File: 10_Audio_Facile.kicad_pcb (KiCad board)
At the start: 2 copper layers, 30.5 x 20.3 mm, 20 parts, among them J1 Conn_01x01, J2 Conn_01x01, J3 Conn_01x01, J4 Conn_01x01, J5 Conn_01x01, J6 Conn_01x01, U1 PAM8302AAS

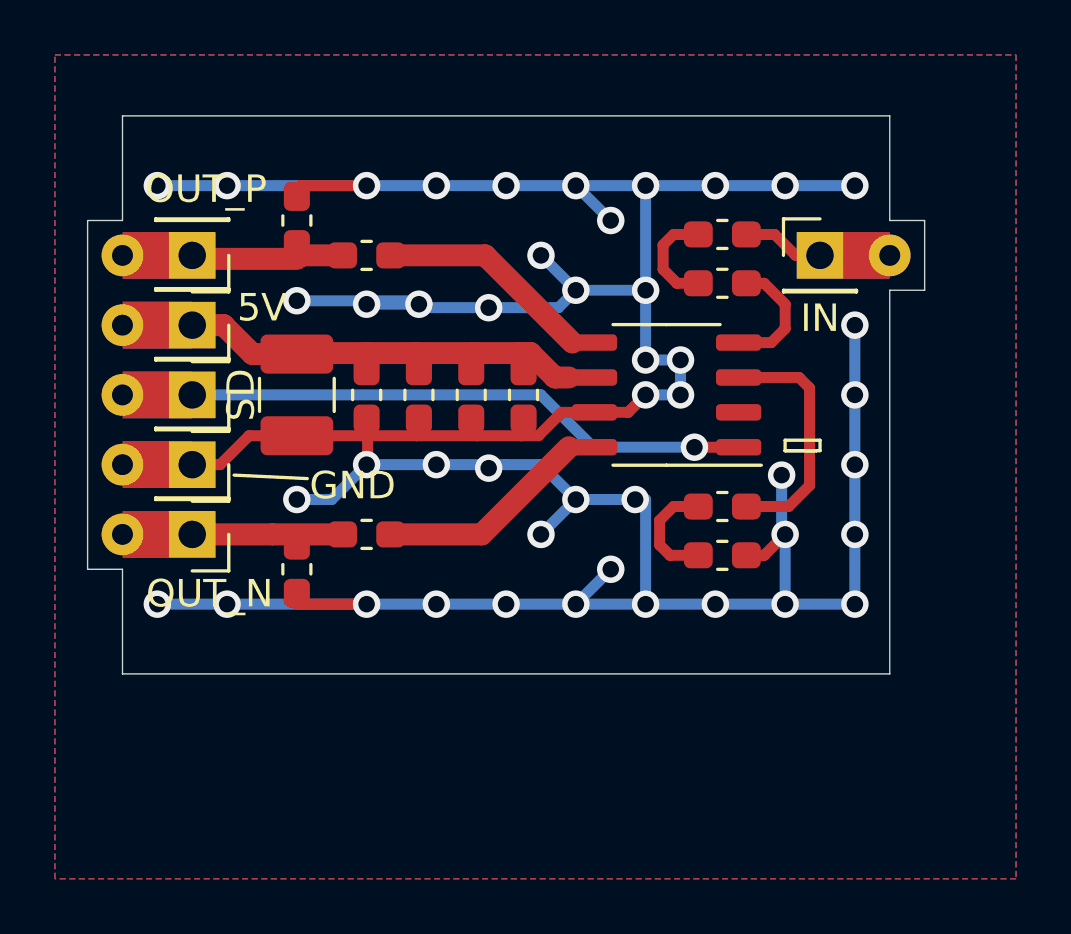
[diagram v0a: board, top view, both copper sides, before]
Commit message: suppression résistances entrées
schéma et routage à jour
raf: optimisation taille de la carte
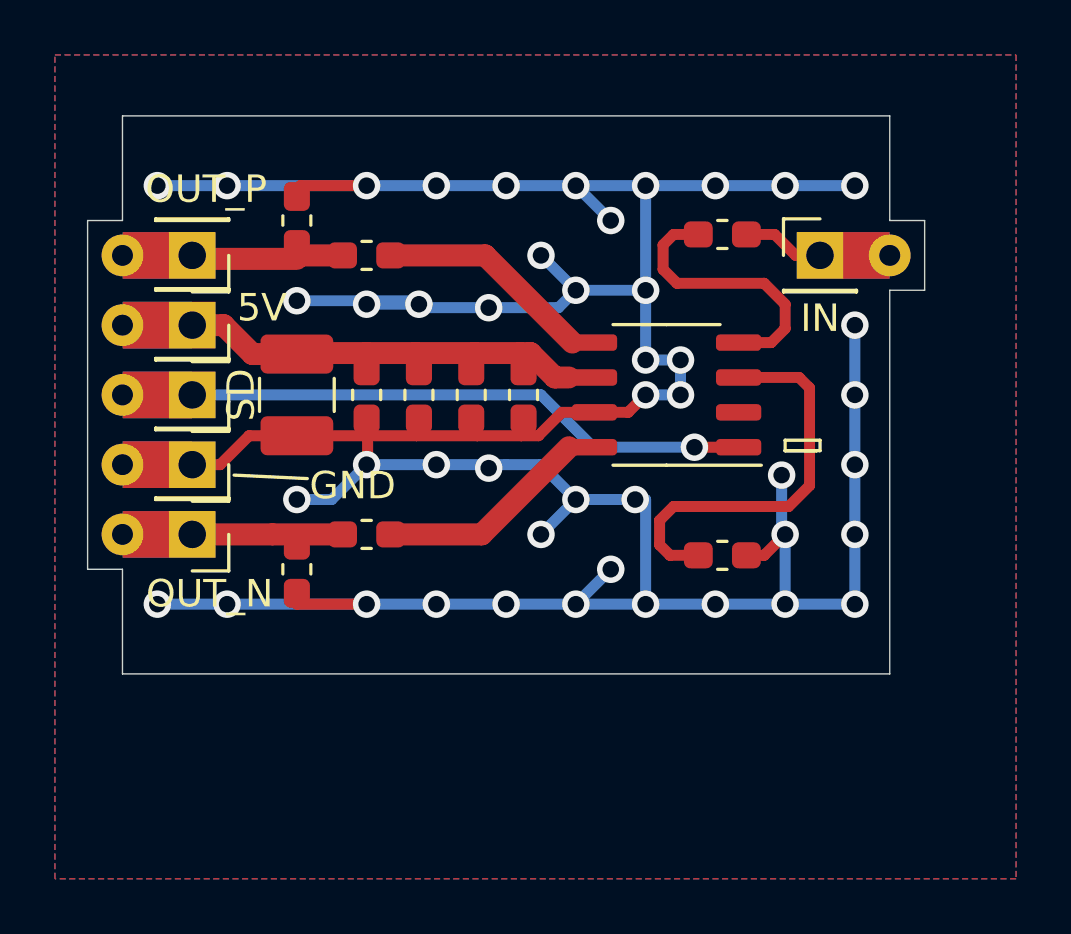
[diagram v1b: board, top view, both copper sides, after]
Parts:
- removed R1, R2: 10k, Resistor_SMD:R_0603_1608Metric_Pad1.05x0.95mm_HandSolder
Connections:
- U1 pad 3: Net-(R1-Pad1) -> Net-(C7-Pad1)
- U1 pad 4: Net-(R2-Pad1) -> Net-(C8-Pad1)
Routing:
- net Net-(C7-Pad1): track 4.08 -> 14.7 mm
- net Net-(R1-Pad1): track 8.91 -> 0.00 mm
- net Net-(C8-Pad1): track 3.83 -> 10.1 mm
- net Net-(R2-Pad1): track 4.52 -> 0.00 mm

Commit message: maj split librairies
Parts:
- J1, J2, J3, J4, J5, J6: footprint Chimere:Castellated_conn -> Chimere_mods:Castellated_conn

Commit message: changement date + generation gerber et fichiers de fabrication
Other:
- board text added: "2021/08/02"
- board text removed: "2021/04/05"
